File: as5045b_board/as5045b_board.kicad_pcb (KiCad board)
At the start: 4 copper layers, 12 parts, among them J10 Conn_01x04, J9 Conn_01x04, U10 AS5045B, U11 AS5045B

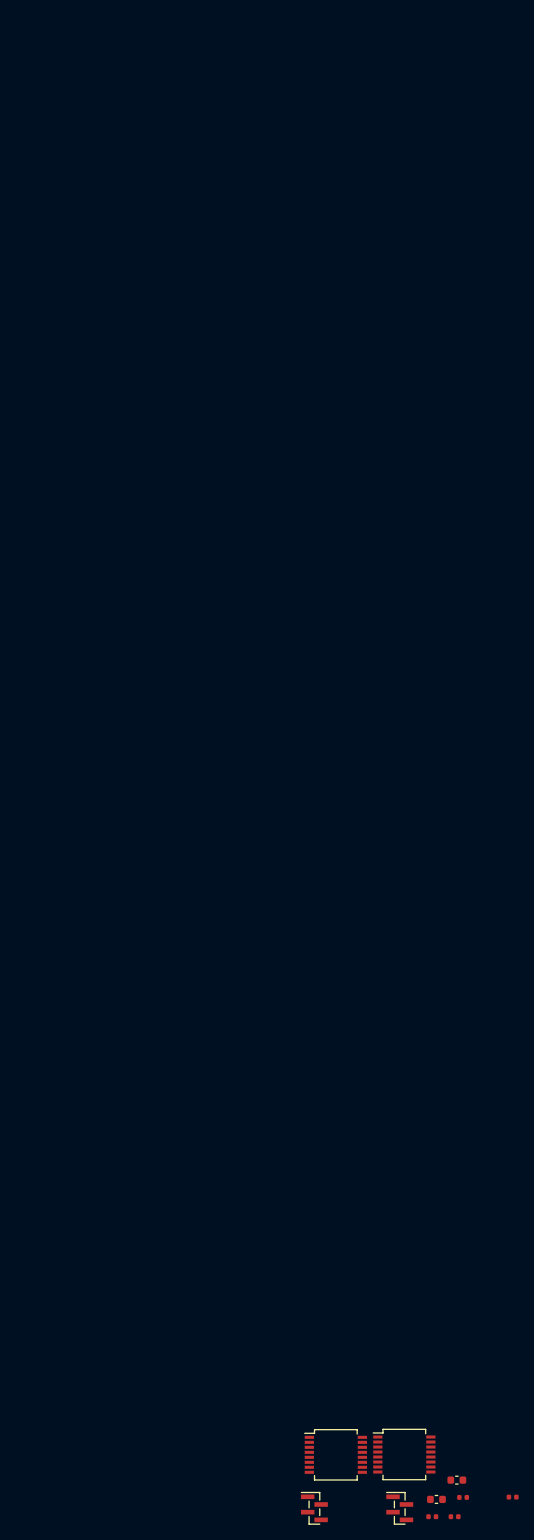
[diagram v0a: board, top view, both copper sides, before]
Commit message: Finished encoders, added XSHUT pullups
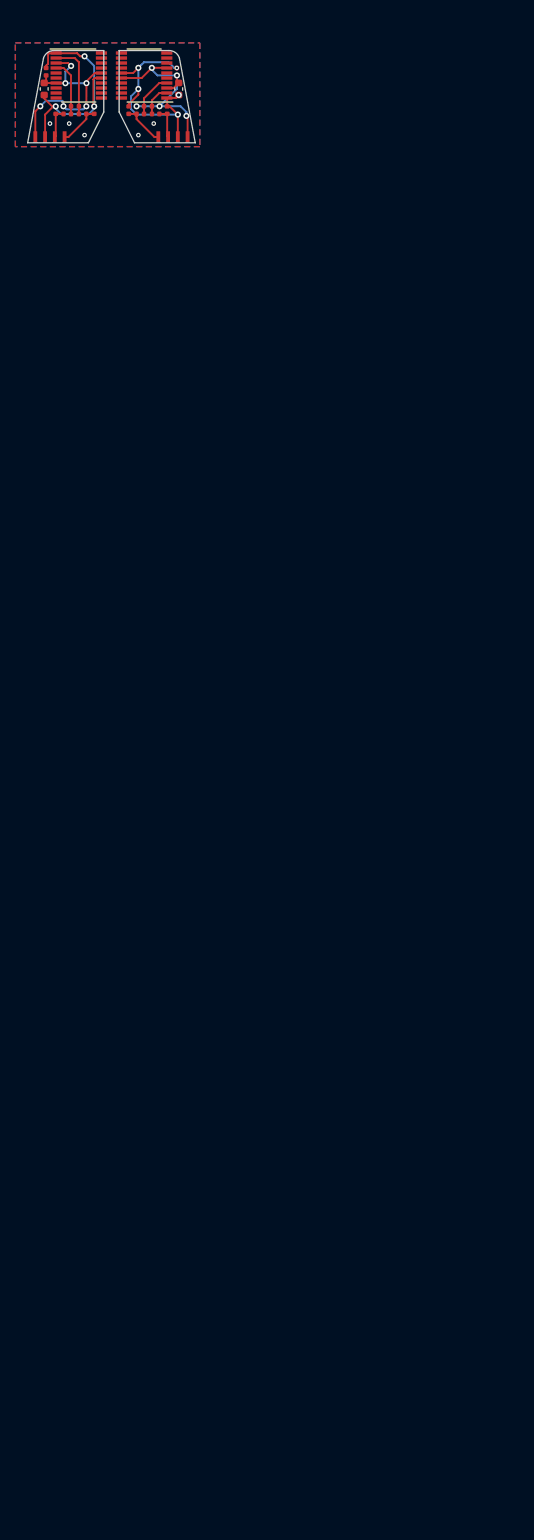
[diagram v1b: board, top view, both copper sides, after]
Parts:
- removed C20, C21: 10uF, Capacitor_SMD:C_0603_1608Metric
- removed C22, C23: 0.1uF, Capacitor_SMD:C_0402_1005Metric
- removed G***: LOGO, synermycha-electronics:Synergia_logo_horizontal_11.4x1.8mm
- removed G***: LOGO, synermycha-electronics:SynerMycha_napis_silk_screen_45.1x17mm
- removed J10, J9: Conn_01x04, Connector_PinHeader_1.00mm:PinHeader_1x04_P1.00mm_Vertical_SMD_Pin1Left
- removed R27, R28: 10K, Resistor_SMD:R_0402_1005Metric
- removed U10, U11: AS5045B, Package_SO:SSOP-16_5.3x6.2mm_P0.65mm
- added C1: 0.1uF, Capacitor_SMD:C_0402_1005Metric, F.Cu at (-11.0, 2.25)
- added C2: 0.1uF, Capacitor_SMD:C_0402_1005Metric, F.Cu at (6.00, 2.25)
- added C3: 10uF, Capacitor_SMD:C_0603_1608Metric, F.Cu at (6.25, 4.50)
- added C4: 10uF, Capacitor_SMD:C_0603_1608Metric, F.Cu at (-11.2, 4.50)
- added J1: Conn_01x04, connector_brd2brd:01x04_1.0x0.5mm_SMD, F.Cu at (5.50, 10.8)
- added J2: Conn_01x04, connector_brd2brd:01x04_1.0x0.5mm_SMD, F.Cu at (-10.5, 10.8)
- added R1: 2K2, Resistor_SMD:R_0402_1005Metric, F.Cu at (1.25, 7.75)
- added R10: 10K, Resistor_SMD:R_0402_1005Metric, F.Cu at (-6.25, 6.75)
- added R11: 10K, Resistor_SMD:R_0402_1005Metric, F.Cu at (1.25, 6.75)
- added R12: 10K, Resistor_SMD:R_0402_1005Metric, F.Cu at (-8.25, 6.75)
- added R2: 3K3, Resistor_SMD:R_0402_1005Metric, F.Cu at (-0.25, 7.25)
- added R3: 2K2, Resistor_SMD:R_0402_1005Metric, F.Cu at (-6.25, 7.75)
- added R4: 3K3, Resistor_SMD:R_0402_1005Metric, F.Cu at (-4.75, 7.25)
- added R5: 2K2, Resistor_SMD:R_0402_1005Metric, F.Cu at (3.25, 7.75)
- added R6: 3K3, Resistor_SMD:R_0402_1005Metric, F.Cu at (4.75, 7.25)
- added R7: 2K2, Resistor_SMD:R_0402_1005Metric, F.Cu at (-8.25, 7.75)
- added R8: 3K3, Resistor_SMD:R_0402_1005Metric, F.Cu at (-9.75, 7.25)
- added R9: 10K, Resistor_SMD:R_0402_1005Metric, F.Cu at (3.25, 6.75)
- added U1: AS5304, Package_SO:TSSOP-20_4.4x6.5mm_P0.65mm, F.Cu at (1.75, 2.75)
- added U2: AS5304, Package_SO:TSSOP-20_4.4x6.5mm_P0.65mm, F.Cu at (-6.75, 2.75)
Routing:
- net GND: track 0.00 -> 62.4 mm, vias 0 -> 13
- net +5V: track 0.00 -> 56.6 mm, vias 0 -> 11
- net Net-(R10-Pad2): track 0.00 -> 9.92 mm
- net Net-(R12-Pad2): track 0.00 -> 7.35 mm
- net Net-(R1-Pad1): track 0.00 -> 5.82 mm
- net Net-(J2-Pad4): track 0.00 -> 5.49 mm
- net Net-(J1-Pad4): track 0.00 -> 5.49 mm
- net Net-(R5-Pad1): track 0.00 -> 4.10 mm
- net Net-(J2-Pad3): track 0.00 -> 4.08 mm
- net Net-(J1-Pad3): track 0.00 -> 4.08 mm
- added copper zone on B.Cu, net GND
- added copper zone on F.Cu, net GND
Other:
- board outline added: 21.8 x 12 mm

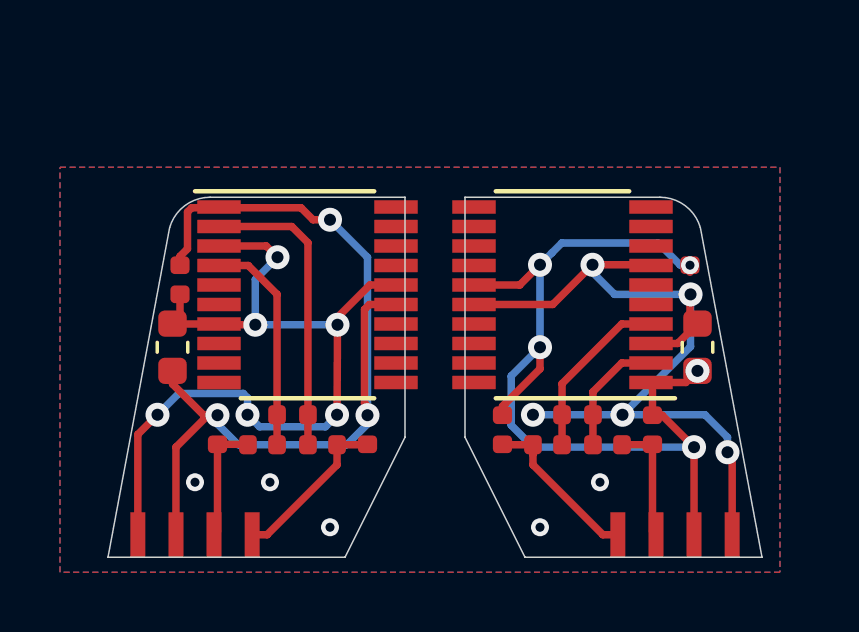
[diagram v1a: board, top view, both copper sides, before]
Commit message: Aktualizacja enkoderów
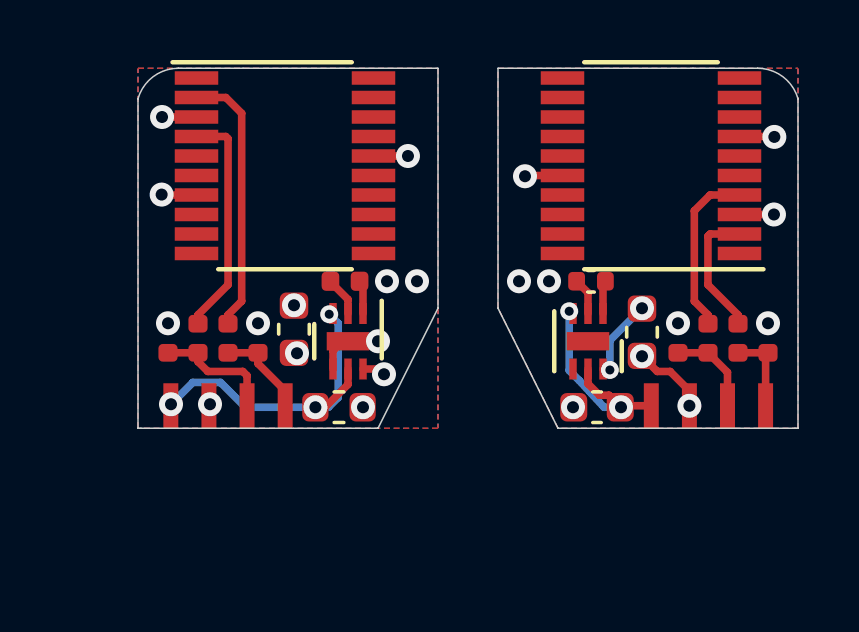
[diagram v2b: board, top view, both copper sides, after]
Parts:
- removed C4: 10uF, Capacitor_SMD:C_0603_1608Metric
- removed R10, R11, R12, R9: 10K, Resistor_SMD:R_0402_1005Metric
- added C5: 2.2uF, Capacitor_SMD:C_0603_1608Metric, F.Cu at (2.90, 6.50)
- added C6: 1uF, Capacitor_SMD:C_0402_1005Metric, F.Cu at (2.70, 2.30)
- added C7: 2.2uF, Capacitor_SMD:C_0603_1608Metric, F.Cu at (-5.70, 6.50)
- added C8: 1uF, Capacitor_SMD:C_0402_1005Metric, F.Cu at (-5.50, 2.30)
- added C9: 4.7uF, Capacitor_SMD:C_0603_1608Metric, F.Cu at (-7.20, 3.90)
- added G***: LOGO, graphics:PinUpGirl_silk_screen_4.4x9.8mm, B.Cu at (4.50, 0.50)
- added G***: LOGO, footprints:dickbutt, B.Cu at (-7.50, -0.50)
- added U3: LTC3221, Package_DFN_QFN:DFN-6-1EP_2x2mm_P0.5mm_EP0.61x1.42mm, F.Cu at (2.60, 4.30)
- added U4: LTC3221, Package_DFN_QFN:DFN-6-1EP_2x2mm_P0.5mm_EP0.61x1.42mm, F.Cu at (-5.40, 4.30)
- C3: value 10uF -> 4.7uF
- moved R2 9.36 mm to (8.60, 4.20)
- moved C1 7.40 mm to (-3.60, 2.30), turned to 180 degrees
- moved R1 7.27 mm to (7.60, 4.20), turned to 270 degrees
- moved U1 5.21 mm to (4.70, -1.55)
- moved C2 5.20 mm to (0.80, 2.30), turned to 0 degrees
- moved R5 4.88 mm to (6.60, 4.20), turned to 270 degrees
- moved R4 4.76 mm to (-8.40, 4.20)
- moved R3 4.75 mm to (-9.40, 4.20), turned to 270 degrees
- moved J1 4.44 mm to (6.62, 6.45), turned to 0 degrees
- moved J2 4.44 mm to (-9.40, 6.45)
- moved U2 4.36 mm to (-7.50, -1.55)
- moved R7 4.15 mm to (-10.4, 4.20), turned to 270 degrees
- moved R8 3.47 mm to (-11.4, 4.20)
- moved R6 3.17 mm to (5.60, 4.20)
- moved C3 1.92 mm to (4.40, 4.00)
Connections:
- J1 pad 1: +5V -> Net-(C5-Pad1)
- J2 pad 1: +5V -> Net-(C7-Pad1)
- U1 pad 2: Net-(R5-Pad1) -> Net-(R1-Pad1)
- U1 pad 20: (no net) -> GND
- U1 pad 4: Net-(R1-Pad1) -> Net-(R5-Pad1)
- U2 pad 20: (no net) -> GND
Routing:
- net GND: track 62.4 -> 4.87 mm
- net +5V: track 56.6 -> 10.6 mm, vias 11 -> 12
- net Net-(C7-Pad1): track 0.00 -> 11.4 mm, vias 0 -> 3
- net Net-(C5-Pad1): track 0.00 -> 7.36 mm, vias 0 -> 2
- net Net-(J1-Pad3): track 5.49 -> 2.80 mm
- net Net-(J2-Pad4): track 5.49 -> 3.14 mm
- net Net-(R5-Pad1): track 4.10 -> 5.68 mm
- net Net-(R1-Pad1): track 5.82 -> 4.41 mm
- net Net-(C8-Pad2): track 0.00 -> 1.32 mm
- net Net-(C6-Pad2): track 0.00 -> 1.23 mm
- net Net-(C8-Pad1): track 0.00 -> 1.12 mm
- net Net-(C6-Pad1): track 0.00 -> 1.11 mm
- net Net-(J1-Pad4): track 4.08 -> 3.03 mm
- net Net-(R3-Pad1): track 9.92 -> 8.93 mm
- added copper zone on In2.Cu, net +5V
- added copper zone on In1.Cu, net GND
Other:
- board size 21.8 x 12 mm -> 22 x 12 mm
- board text removed: "BY"
